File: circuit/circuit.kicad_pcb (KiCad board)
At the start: 2 copper layers, 40 x 29 mm, 32 parts, among them IC1 BNO085, J3 USB_C_Receptacle_USB2.0, J4 Conn_01x10_Pin, U1 ESP32-C3-WROOM-02, U2 BD33FC0FP

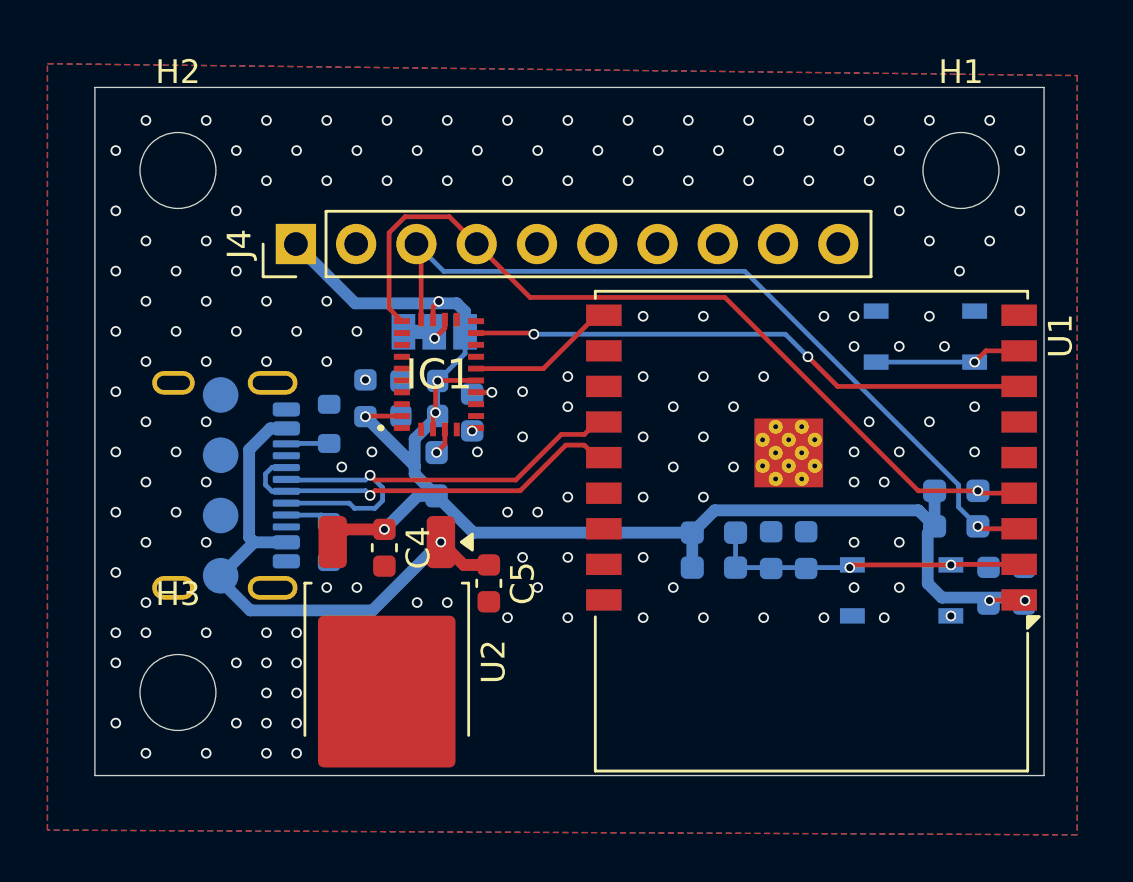
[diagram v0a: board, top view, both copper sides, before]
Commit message: delete pad on via
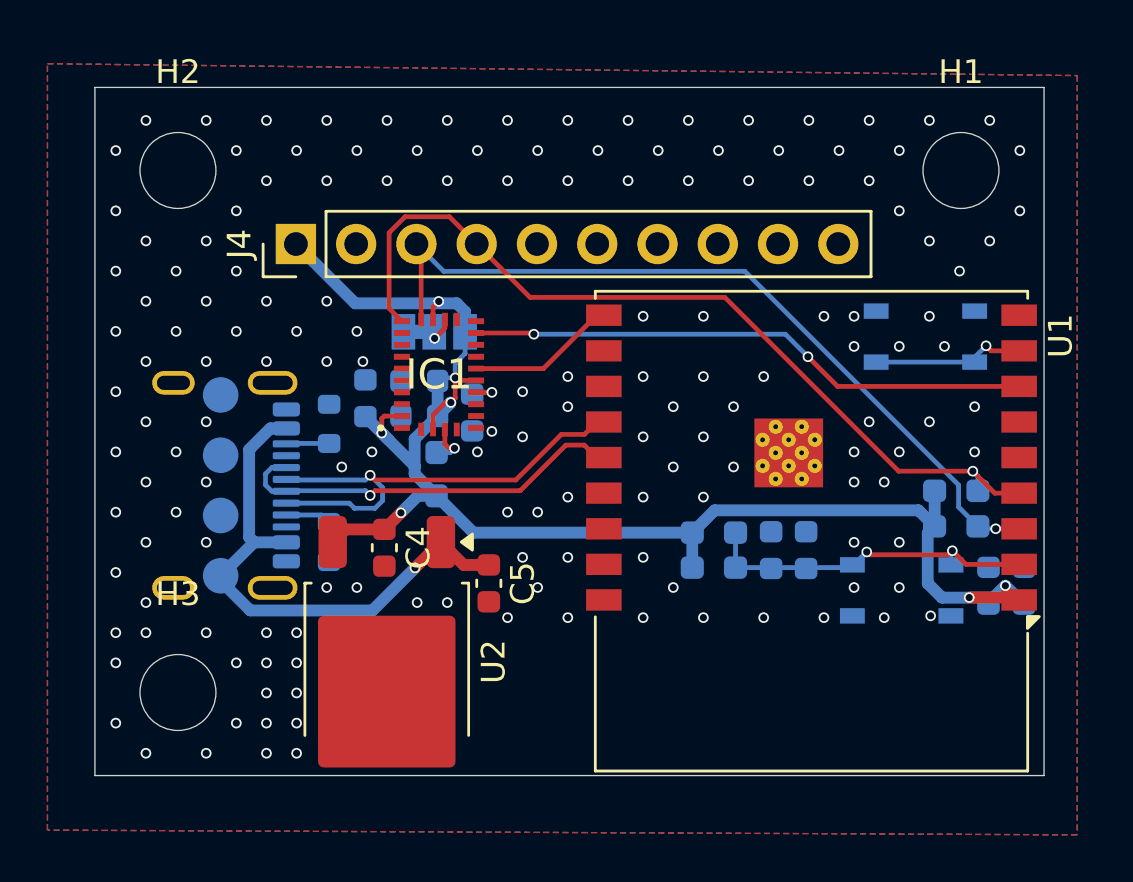
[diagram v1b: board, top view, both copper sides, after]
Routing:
- net +3.3V: track 65.4 -> 68.6 mm
- net NRST: track 13.6 -> 15.5 mm
- net SDA: track 35.6 -> 36.5 mm
- net Net-(IC1-BOOTN): track 1.12 -> 1.93 mm

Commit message: a
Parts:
- renumbered NRST1 to RST, button1 to boot
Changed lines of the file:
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@@
 			(at 0 -4.15 0)
 			(layer "F.SilkS")
+			(hide yes)
 			(effects
 				(font
@@
 		(tags "capacitor")
 		(property "Reference" "C4"
-			(at 0 -1.43 90)
+			(at -2.5668 -0.0084 90)
 			(layer "F.SilkS")
 			(effects
@@
 		(tags "Integrated Circuit")
 		(property "Reference" "IC1"
-			(at 0 0 0)
+			(at 0.0056 -3.4632 0)
 			(layer "F.SilkS")
 			(effects
@@
 			(at 0 -4.15 0)
 			(layer "F.SilkS")
+			(hide yes)
 			(effects
 				(font
@@
 			(at -10.5 5.13 90)
 			(layer "F.SilkS")
+			(hide yes)
 			(effects
 				(font
@@
 			(at 0 -4.15 0)
 			(layer "F.SilkS")
+			(hide yes)
 			(effects
 				(font
@@
 		(tags "capacitor")
 		(property "Reference" "C9"
-			(at 0 1.43 90)
+			(at 1.4992 -1.4776 90)
 			(layer "B.SilkS")
 			(effects
@@
 			(at 0 1.648 180)
 			(layer "B.SilkS")
+			(hide yes)
 			(effects
 				(font
@@
 			(at 0 1.648 180)
 			(layer "B.SilkS")
+			(hide yes)
 			(effects
 				(font
@@
 			(at 0 1.648 180)
 			(layer "B.SilkS")
+			(hide yes)
 			(effects
 				(font
@@
 		(tags "resistor")
 		(property "Reference" "R23"
-			(at 0 1.43 90)
+			(at 0 -1.4728 90)
 			(layer "B.SilkS")
 			(effects
@@
 		(tags "capacitor")
 		(property "Reference" "C2"
-			(at 0 1.43 90)
+			(at -5.9448 0.5088 90)
 			(layer "B.SilkS")
 			(effects
@@
 		(descr "C&K Components, PTS 810 Series, Microminiature SMT Top Actuated, http://www.ckswitches.com/media/1476/pts810.pdf")
 		(tags "SPST Button Switch")
-		(property "Reference" "NRST1"
-			(at 0 2.6 0)
+		(property "Reference" "RST"
+			(at -4.926 0.8148 0)
 			(layer "B.SilkS")
 			(effects
@@
 		(tags "resistor handsolder")
 		(property "Reference" "R1"
-			(at 0 1.43 0)
+			(at 2.601 -0.0002 0)
 			(layer "B.SilkS")
 			(effects
@@
 		(descr "C&K Components, PTS 810 Series, Microminiature SMT Top Actuated, http://www.ckswitches.com/media/1476/pts810.pdf")
 		(tags "SPST Button Switch")
-		(property "Reference" "button1"
+		(property "Reference" "boot"
 			(at 0 2.6 0)
 			(layer "B.SilkS")
@@
 		(tags "capacitor")
 		(property "Reference" "C23"
-			(at 0 1.43 90)
+			(at 1.854 1.5392 90)
 			(layer "B.SilkS")
 			(effects
@@
 		(tags "resistor handsolder")
 		(property "Reference" "R3"
-			(at 0 1.43 0)
+			(at -2.6032 -0.0144 0)
 			(layer "B.SilkS")
 			(effects
@@
 		(tags "resistor handsolder")
 		(property "Reference" "R6"
-			(at 0 1.43 0)
+			(at 2.601 -0.0002 0)
 			(layer "B.SilkS")
 			(effects
@@
 		(tags "resistor handsolder")
 		(property "Reference" "R4"
-			(at 0 1.43 0)
+			(at -2.6032 0.0604 0)
 			(layer "B.SilkS")
 			(effects
@@
 			(at 0 1.648 180)
 			(layer "B.SilkS")
+			(hide yes)
 			(effects
 				(font
@@
 		(tags "capacitor")
 		(property "Reference" "C7"
-			(at 0 1.43 0)
+			(at 2.4268 1.7344 0)
 			(layer "B.SilkS")
 			(effects
@@
 		(tags "capacitor")
 		(property "Reference" "C8"
-			(at 0 1.43 0)
+			(at 0.852 -1.5168 0)
 			(layer "B.SilkS")
 			(effects
@@
 			(at 0 1.8 0)
 			(layer "B.SilkS")
+			(hide yes)
 			(effects
 				(font
@@
 			(layer "B.CrtYd")
 		)
-		(fp_text user "3"
-			(at 2.6 0 0)
-			(layer "B.SilkS")
-			(effects
-				(font
-					(size 1 1)
-					(thickness 0.15)
-				)
-				(justify mirror)
-			)
-		)
-		(fp_text user "1"
-			(at -2.6 0 0)
-			(layer "B.SilkS")
-			(effects
-				(font
-					(size 1 1)
-					(thickness 0.15)
-				)
-				(justify mirror)
-			)
-		)
 		(pad "1" smd rect
 			(at -1.3 0)
@@
 		(tags "capacitor")
 		(property "Reference" "C3"
-			(at 0 1.43 90)
+			(at -5.9448 0.3832 90)
 			(layer "B.SilkS")
 			(effects
@@
 		(tags "capacitor")
 		(property "Reference" "C1"
-			(at 0 1.43 90)
+			(at 2.108 0.0152 90)
 			(layer "B.SilkS")
 			(effects
@@
 		(tags "resistor")
 		(property "Reference" "R24"
-			(at 0 1.43 90)
+			(at -1.892 1.5236 90)
 			(layer "B.SilkS")
 			(effects
